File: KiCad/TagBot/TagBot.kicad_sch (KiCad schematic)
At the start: 23 parts, among them J1 Conn_ST_STDC14, U1 STM32G431CBUx, Y1 Crystal

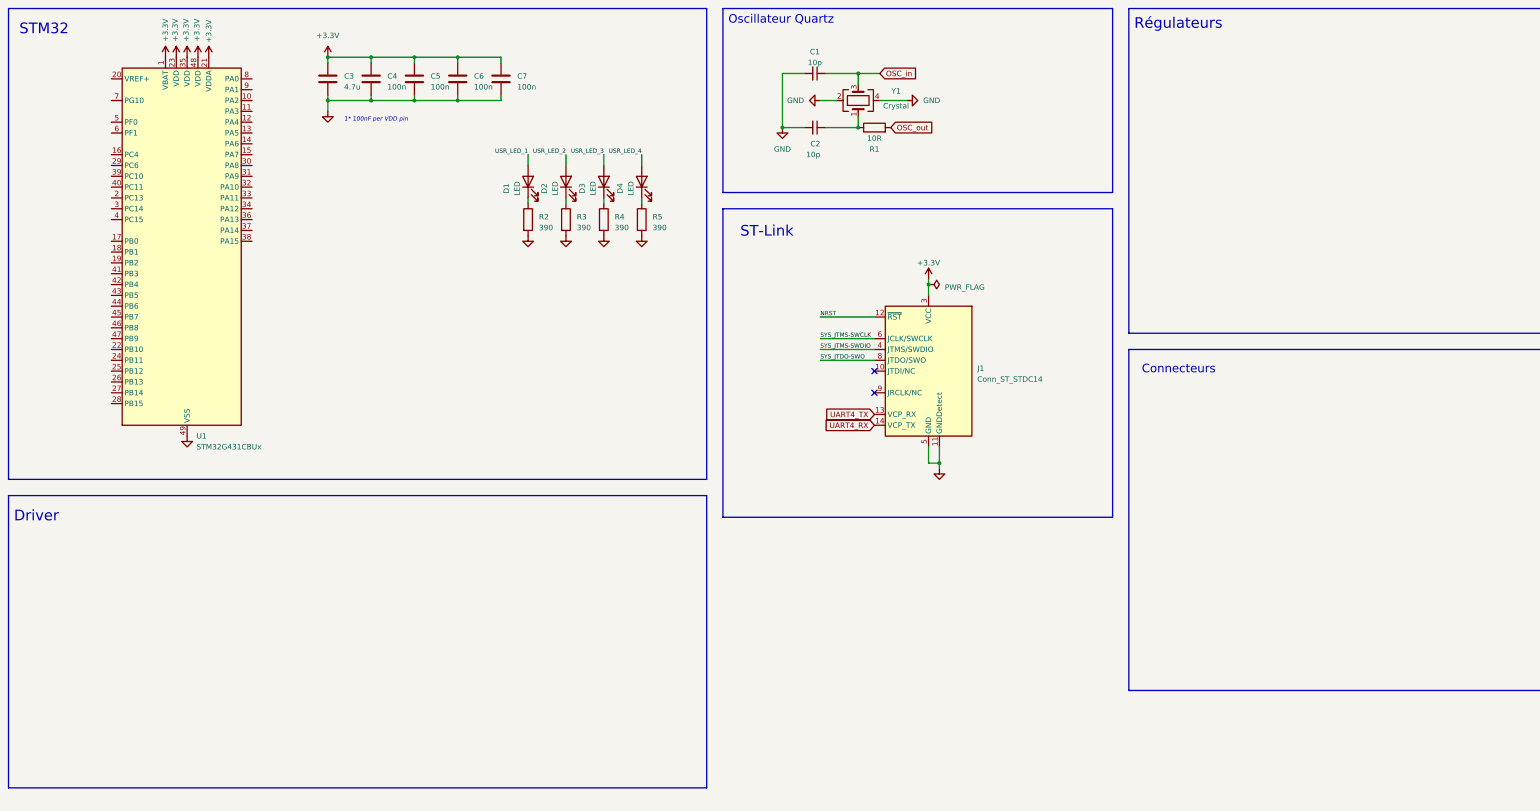
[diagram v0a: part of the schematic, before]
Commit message: kicad and cubeide pin config
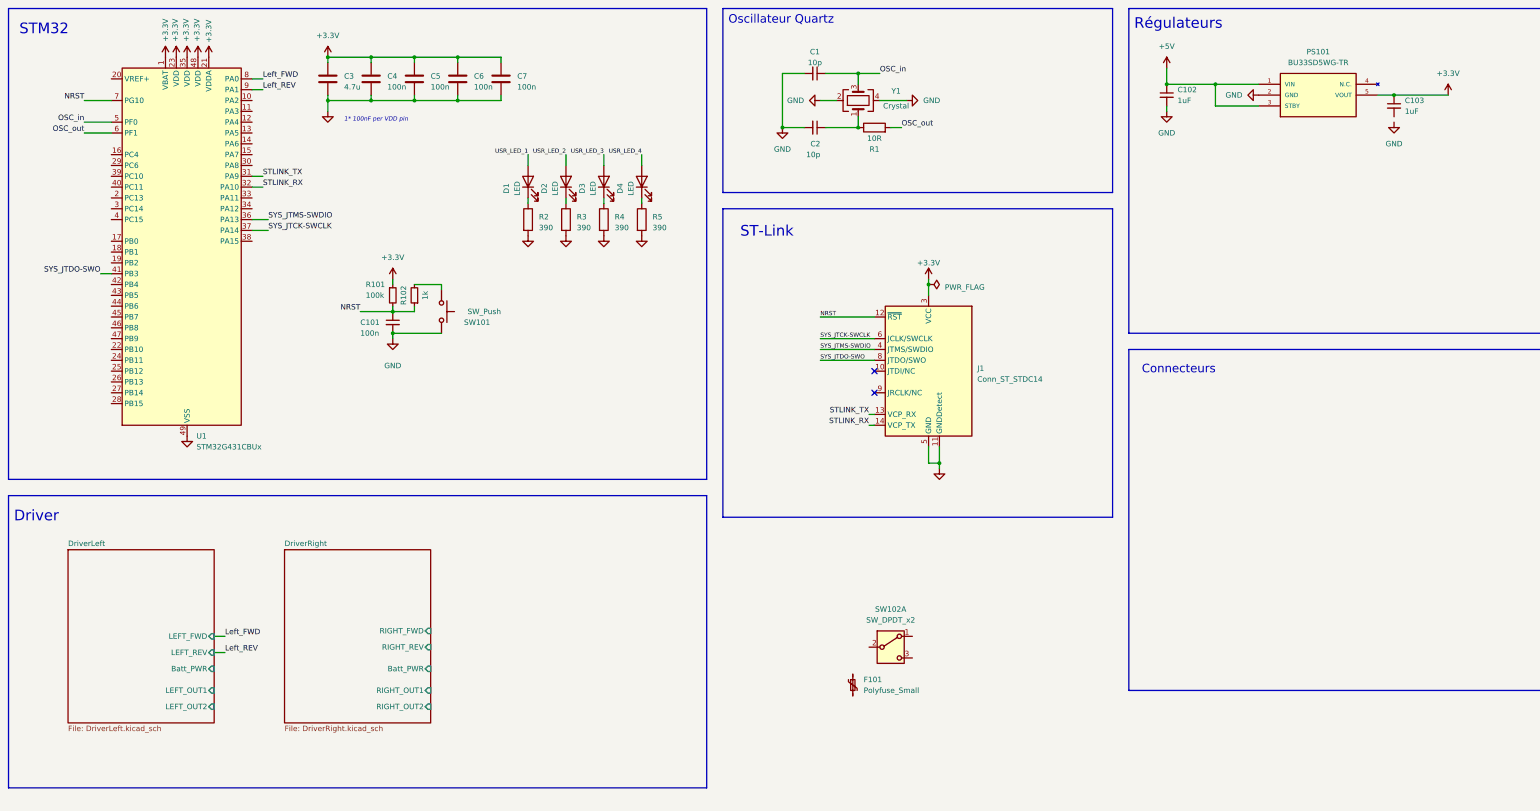
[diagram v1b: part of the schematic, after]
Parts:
- added C101: 100n, Capacitor_SMD:C_0402_1005Metric, symbol Device:C_Small
- added C102, C103: 1uF, symbol Device:C_Small
- added F101: Polyfuse_Small, symbol Device:Polyfuse_Small
- added PS101: BU33SD5WG-TR, BU33SD5WG-TR:SOT95P280X125-5N, symbol BU33SD5WG-TR:BU33SD5WG-TR
- added R101: 100k, Resistor_SMD:R_0402_1005Metric, symbol Device:R_Small
- added R102: 1k, Resistor_SMD:R_0402_1005Metric, symbol Device:R_Small
- added SW101: SW_Push, Button_Switch_SMD:SW_SPST_B3U-1000P, symbol Switch:SW_Push
- added SW102: SW_DPDT_x2, symbol Switch:SW_DPDT_x2
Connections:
- net SYS_JTMS-SWCLK is gone; now on net SYS_JTCK-SWCLK: J1.6 (JCLK/SWCLK)
- net UART4_RX is gone; now on net STLINK_RX: J1.14 (VCP_TX)
- net UART4_TX is gone; now on net STLINK_TX: J1.13 (VCP_RX)
- net +3.3V: now also C103.1, PS101.5 (VOUT), R101.1
- net GND: now also C101.2, C102.2, PS101.2 (GND), SW101.2
- net NRST: now also U1.7 (PG10), C101.1, R101.2, R102.1
- net OSC_in: now also U1.5 (PF0)
- net OSC_out: now also U1.6 (PF1)
- net SYS_JTDO-SWO: now also U1.41 (PB3)
- net SYS_JTMS-SWDIO: now also U1.36 (PA13)
- net STLINK_TX: now reaches U1.31 (PA9)
- net STLINK_RX: now reaches U1.32 (PA10)
- net SYS_JTCK-SWCLK: now reaches U1.37 (PA14)
- net Left_FWD: now reaches U1.8 (PA0)
- net Left_REV: now reaches U1.9 (PA1)
- new net: R102.2, SW101.1
- new net +5V: C102.1, PS101.1 (VIN), PS101.3 (STBY)
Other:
- added sheet DriverLeft (DriverLeft.kicad_sch)
- added sheet DriverRight (DriverRight.kicad_sch)

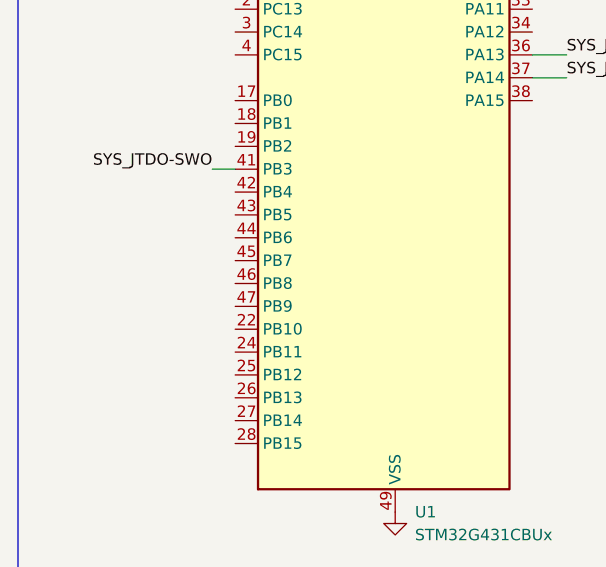
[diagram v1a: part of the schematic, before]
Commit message: boot0 of stm32 connected to gnd
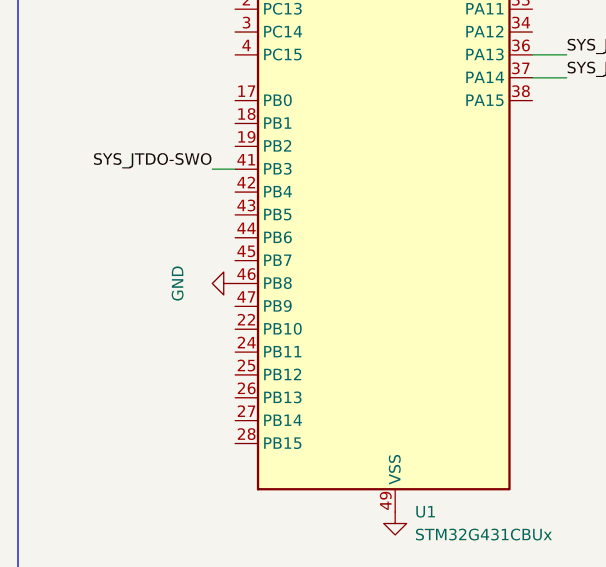
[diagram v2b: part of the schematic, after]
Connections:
- net GND: now also U1.46 (PB8)
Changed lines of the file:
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@@
+	)
+	(symbol
+		(lib_id "power:GND")
+		(at 39.37 90.17 270)
+		(unit 1)
+		(exclude_from_sim no)
+		(in_bom yes)
+		(on_board yes)
+		(dnp no)
+		(property "Reference" "#PWR0108"
+			(at 33.02 90.17 0)
+			(effects
+				(font
+					(size 1.27 1.27)
+				)
+				(hide yes)
+			)
+		)
+		(property "Value" "GND"
+			(at 33.02 90.17 0)
+			(effects
+				(font
+					(size 1.27 1.27)
+				)
+			)
+		)
+		(property "Footprint" ""
+			(at 39.37 90.17 0)
+			(effects
+				(font
+					(size 1.27 1.27)
+				)
+				(hide yes)
+			)
+		)
+		(property "Datasheet" ""
+			(at 39.37 90.17 0)
+			(effects
+				(font
+					(size 1.27 1.27)
+				)
+				(hide yes)
+			)
+		)
+		(property "Description" ""
+			(at 39.37 90.17 0)
+			(effects
+				(font
+					(size 1.27 1.27)
+				)
+				(hide yes)
+			)
+		)
+		(pin "1"
+		)
+		(instances
+			(project "TagBot"
+				(path "/6db08f37-7cb3-4000-93f1-ba0d0ffbeb19"
+					(reference "#PWR0108")
+					(unit 1)
+				)
+			)
+		)
 	)
 	(symbol

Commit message: update kicad
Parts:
- removed C101: 100n, Capacitor_SMD:C_0402_1005Metric, symbol Device:C_Small
- removed R101: 100k, Resistor_SMD:R_0402_1005Metric, symbol Device:R_Small
- removed R102: 1k, Resistor_SMD:R_0402_1005Metric, symbol Device:R_Small
- removed SW101: SW_Push, Button_Switch_SMD:SW_SPST_B3U-1000P, symbol Switch:SW_Push
- added C? (x2): 1µF, symbol Device:C_Small
- added C?: 100n, Capacitor_SMD:C_0402_1005Metric, symbol Device:C_Small
- added D? (x2): LED, LED_SMD:LED_0603_1608Metric, symbol Device:LED
- added IC?: ADXL343BCCZ-RL, ADXL343BCCZRL, symbol ADXL343BCCZ-RL:ADXL343BCCZ-RL
- added J?: Conn_01x02, Connector_AMASS:AMASS_XT60-F_1x02_P7.20mm_Vertical, symbol Connector_Generic:Conn_01x02
- added R?: 1.5k, Resistor_SMD:R_0402_1005Metric, symbol Device:R_Small
- added R?: 100k, Resistor_SMD:R_0402_1005Metric, symbol Device:R_Small
- added R?: 1k, Resistor_SMD:R_0402_1005Metric, symbol Device:R_Small
- added R?: 220, Resistor_SMD:R_0402_1005Metric, symbol Device:R_Small
- added SW?: SW_Push, Button_Switch_SMD:SW_SPST_B3U-1000P, symbol Switch:SW_Push
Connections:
- net +3.3V: now also C?.1, C?.1, C?.2, C?.2, IC?.1 (VDD_I/O), IC?.6 (VS), R?.1, R?.1
- net GND: now also C?.2, D?.1 (K), D?.1 (K), IC?.2 (GND_1), IC?.4 (GND_2), IC?.5 (GND_3), J?.1 (Pin_1), SW?.2
- net NRST: now also C?.1, R?.1, R?.2
- net CS-NSS: now reaches U1.12 (PA4)
- net CS-NSS: now also IC?.7 (~{CS})
- net SCLK-SCK: now reaches U1.13 (PA5)
- net SCLK-SCK: now also IC?.14 (SCL/SCLK)
- net SDO-MISO: now reaches U1.14 (PA6)
- net SDO-MISO: now also IC?.12 (SDO/ALT_ADDRESS)
- net SDI-MOSI: now reaches U1.15 (PA7)
- net SDI-MOSI: now also IC?.13 (SDA/SDI/SDIO)
- net Right_REV: now reaches U1.34 (PA12)
- net LIDAR_Input: now reaches U1.39 (PC10)
- net LIDAR_Output: now reaches U1.40 (PC11)
- net LPTIM1_IN1: now reaches U1.43 (PB5)
- net Right_FWD: now reaches U1.44 (PB6)
- net LPTIM1_IN2: now reaches U1.45 (PB7)
- new net: D?.2 (A), R?.2 (x2)
- new net: R?.2, SW?.1
- new net 7.2V: J?.2 (Pin_2), R?.1
- no-connect marks 2 -> 7
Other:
- note added: "Accéléromètre"
- note added: "Batterie"
- note added: "Connecteurs (LIDAR, batterie, moteurs (left and right), capteur fin de bords)"
- note added: "Drivers"
- note added: "Switch"
- note removed: "Connecteurs"
- note removed: "Driver"
- moved on the sheet: F101, SW102A

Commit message: update kicad
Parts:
- removed C102, C103: 1uF, symbol Device:C_Small
- removed C?: 100n, Capacitor_SMD:C_0402_1005Metric, symbol Device:C_Small
- removed D? (x2): LED, LED_SMD:LED_0603_1608Metric, symbol Device:LED
- removed F101: Polyfuse_Small, symbol Device:Polyfuse_Small
- removed J?: Conn_01x02, Connector_AMASS:AMASS_XT60-F_1x02_P7.20mm_Vertical, symbol Connector_Generic:Conn_01x02
- removed PS101: BU33SD5WG-TR, BU33SD5WG-TR:SOT95P280X125-5N, symbol BU33SD5WG-TR:BU33SD5WG-TR
- removed R?: 1.5k, Resistor_SMD:R_0402_1005Metric, symbol Device:R_Small
- removed R?: 100k, Resistor_SMD:R_0402_1005Metric, symbol Device:R_Small
- removed R?: 1k, Resistor_SMD:R_0402_1005Metric, symbol Device:R_Small
- removed R?: 220, Resistor_SMD:R_0402_1005Metric, symbol Device:R_Small
- removed SW102: SW_DPDT_x2, symbol Switch:SW_DPDT_x2
- removed SW?: SW_Push, Button_Switch_SMD:SW_SPST_B3U-1000P, symbol Switch:SW_Push
- added C? (x2): 100n, Capacitor_SMD:C_0402_1005Metric, symbol Device:C_Small
- added C?: 100nF, symbol Device:C_Small
- added D?: LED, LED_SMD:LED_0603_1608Metric, symbol Device:LED
- added J102, J104: Conn_01x06, symbol Connector_Generic:Conn_01x06
- added J? (x2): Conn_01x02, Connector_AMASS:AMASS_XT60-F_1x02_P7.20mm_Vertical, symbol Connector_Generic:Conn_01x02
- added J?: Conn_01x04, symbol Connector_Generic:Conn_01x04
- added J?: Conn_01x08, symbol Connector_Generic:Conn_01x08
- added J? (x4): Conn_01x03, symbol Connector_Generic:Conn_01x03
- added JP? (x3): SolderJumper_2_Open, symbol Jumper:SolderJumper_2_Open
- added R? (x2): 100k, Resistor_SMD:R_0402_1005Metric, symbol Device:R_Small
- added R? (x2): 1k, Resistor_SMD:R_0402_1005Metric, symbol Device:R_Small
- added R?: 1.5k, Resistor_SMD:R_0402_1005Metric, symbol Device:R_Small
- added SW?: SW_SPDT_312, symbol Switch:SW_SPDT_312
- added Wurth 430182070816: SW_Push, Button_Switch_SMD:SW_Push_1P1T_NO_6x6mm_H9.5mm, symbol Switch:SW_Push (x2)
- gave numbers to parts that had none: 3
- renumbered C3 to C103, C4 to C104, C5 to C105, C6 to C106, C7 to C107, C1 to C109, C2 to C110, D1 to D101, D2 to D102, D3 to D103, D4 to D104, H1 to H101, H2 to H102, H3 to H103, H4 to H104, J1 to J101, R2 to R101, R3 to R102, R4 to R103, R5 to R104, R1 to R107, U1 to U101, Y1 to Y101
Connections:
- net USR_LED_3 is gone; now on net USR_LED_1: D103.2 (A)
- net USR_LED_4 is gone; now on net USR_LED_2: D104.2 (A)
- net +3.3V: now also U101.20 (VREF+), C?.1, C?.2, R?.1, R?.1
- net +5V: now also J102.5 (Pin_5), J104.5 (Pin_5), J?.3 (Pin_3), J?.3 (Pin_3), J?.3 (Pin_3), J?.3 (Pin_3), J?.8 (Pin_8)
- net 7.2V: now also R?.1, SW?.1 (B)
- net GND: now also C?.2, C?.2, D?.1 (K), J102.2 (Pin_2), J104.2 (Pin_2), J?.1 (Pin_1), J?.1 (Pin_1), J?.2 (Pin_2), J?.2 (Pin_2), J?.2 (Pin_2), J?.2 (Pin_2), J?.5 (Pin_5), Wurth 430182070816.2, Wurth 430182070816.2
- net LIDAR_Input: now also U101.22 (PB10), J?.6 (Pin_6); no longer U101.39 (PC10)
- net LIDAR_Output: now also U101.24 (PB11), J?.7 (Pin_7); no longer U101.40 (PC11)
- net Left_FWD: now also U101.32 (PA10); no longer U101.8 (PA0)
- net Left_REV: now also U101.33 (PA11); no longer U101.9 (PA1)
- net NRST: now also C?.1, R?.1, R?.2
- net Right_FWD: now also U101.30 (PA8); no longer U101.44 (PB6)
- net Right_REV: now also U101.31 (PA9); no longer U101.34 (PA12)
- net STLINK_RX: now also U101.40 (PC11); no longer U101.32 (PA10)
- net STLINK_TX: now also U101.39 (PC10); no longer U101.31 (PA9)
- net USR_LED_1: now also U101.8 (PA0); no longer D101.2 (A)
- net USR_LED_2: now also U101.9 (PA1); no longer D102.2 (A)
- net Interrupt1: now reaches U101.10 (PA2)
- net Interrupt1: now also IC101.9 (INT2)
- net Interrupt2: now reaches U101.11 (PA3)
- net Interrupt2: now also IC101.8 (INT1)
- net M_EN: now reaches U101.16 (PC4)
- net M_EN: now also JP?.1 (A)
- net DEV_EN: now reaches U101.17 (PB0)
- net DEV_EN: now also JP?.1 (A)
- net M_SCTR: now reaches U101.18 (PB1)
- net M_SCTR: now also JP?.1 (A)
- net Capteur_dist_S: now reaches U101.19 (PB2)
- net Capteur_dist_S: now also J?.1 (Pin_1)
- net LED_chat: now reaches U101.2 (PC13)
- net LED_chat: now also D101.2 (A)
- net Capteur_dist_N: now reaches U101.25 (PB12)
- net Capteur_dist_N: now also J?.1 (Pin_1)
- net Capteur_dist_W: now reaches U101.27 (PB14)
- net Capteur_dist_W: now also J?.1 (Pin_1)
- net Capteur_dist_E: now reaches U101.28 (PB15)
- net Capteur_dist_E: now also J?.1 (Pin_1)
- net LED_souris: now reaches U101.3 (PC14)
- net LED_souris: now also D102.2 (A)
- net OLED_SCL: now reaches U101.38 (PA15)
- net Encoder_Right_A: now reaches U101.42 (PB4)
- net Encoder_Right_A: now also J104.3 (Pin_3)
- net OLED_SDA: now reaches U101.47 (PB9)
- net LPTIM1_IN1 renamed Encoder_Right_B
- net Encoder_Right_B: now also J104.4 (Pin_4)
- net LPTIM1_IN2 renamed Encoder_Left_B
- net Encoder_Left_B: now also J102.4 (Pin_4)
- new net: R?.2, Wurth 430182070816.1 (x2)
- new net: C?.1, R?.1, R?.2
- new net: J?.4 (Pin_4), JP?.2 (B)
- new net: D?.2 (A), R?.2
- new net: J?.2 (Pin_2), JP?.2 (B)
- new net: J?.3 (Pin_3), JP?.2 (B)
- new net Encoder_Left_A: J102.3 (Pin_3), U101.44 (PB6)
- new net LEFT_OUT1: J102.1 (Pin_1)
- new net LEFT_OUT2: J102.6 (Pin_6)
- new net RIGHT_OUT1: J104.1 (Pin_1)
- new net RIGHT_OUT2: J104.6 (Pin_6)
- new net Vbatterie: J?.2 (Pin_2), SW?.3 (A)
- new net Vcharge: J?.2 (Pin_2), SW?.2 (C)
- no-connect marks 7 -> 10
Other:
- added sheet Régulateur 3.3V (regulateur3.3V.kicad_sch)
- added sheet Régulateur 5V (regulateur5V.kicad_sch)
- note added: "Chargeur NiMH"
- note added: "Connecteurs"
- note added: "LIDAR"
- note added: "capteurs fin de bords"
- note added: "moteurs (left)"
- note added: "moteurs (right)"
- note added: "écran"
- note removed: "Connecteurs (LIDAR, batterie, moteurs (left and right), capteur fin de bords)"
- note removed: "Switch"
- moved on the sheet: C103, C104, C105, C106, C107, D101, D102, D103, D104, H101, H102, H103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

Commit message: update kicad
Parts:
- removed C?: 100n, Capacitor_SMD:C_0402_1005Metric, symbol Device:C_Small
- removed R?: 100k, Resistor_SMD:R_0402_1005Metric, symbol Device:R_Small
- removed R?: 1k, Resistor_SMD:R_0402_1005Metric, symbol Device:R_Small
- removed Wurth 430182070816: SW_Push, Button_Switch_SMD:SW_Push_1P1T_NO_6x6mm_H9.5mm, symbol Switch:SW_Push
- added C112: 100n, Capacitor_SMD:C_0402_1005Metric, symbol Device:C_Small
- added R106: 100k, Resistor_SMD:R_0402_1005Metric, symbol Device:R_Small
- added R109: 1k, Resistor_SMD:R_0402_1005Metric, symbol Device:R_Small
- added SW102: SW_Push, Button_Switch_SMD:SW_Push_1P1T_NO_6x6mm_H9.5mm, symbol Switch:SW_Push
- SW101: renamed from Wurth 430182070816
- gave numbers to parts that had none: 18
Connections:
- net +3.3V: now also R106.1
- net GND: now also C112.2, SW102.2
- net BTN_CAT_MOUSE: now reaches U101.4 (PC15)
- net BTN_CAT_MOUSE: now also C112.1, R106.2, R109.1
- new net: R109.2, SW102.1
- no-connect marks 10 -> 9
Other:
- moved on the sheet: C111, D101, D102, D103, D104, R101, R102, R103, R104, R105, R108
